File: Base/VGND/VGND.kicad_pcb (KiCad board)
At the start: 2 copper layers, 30 x 84 mm, 36 parts, among them J1 Barrel_Jack_Switch, J2 Conn_01x04_Pin, J3 Conn_01x05_Pin, J4 AudioJack2_Ground, J5 AudioJack2_Ground, Q1 40V, U1 TLE2426xD, U2 OPA1656

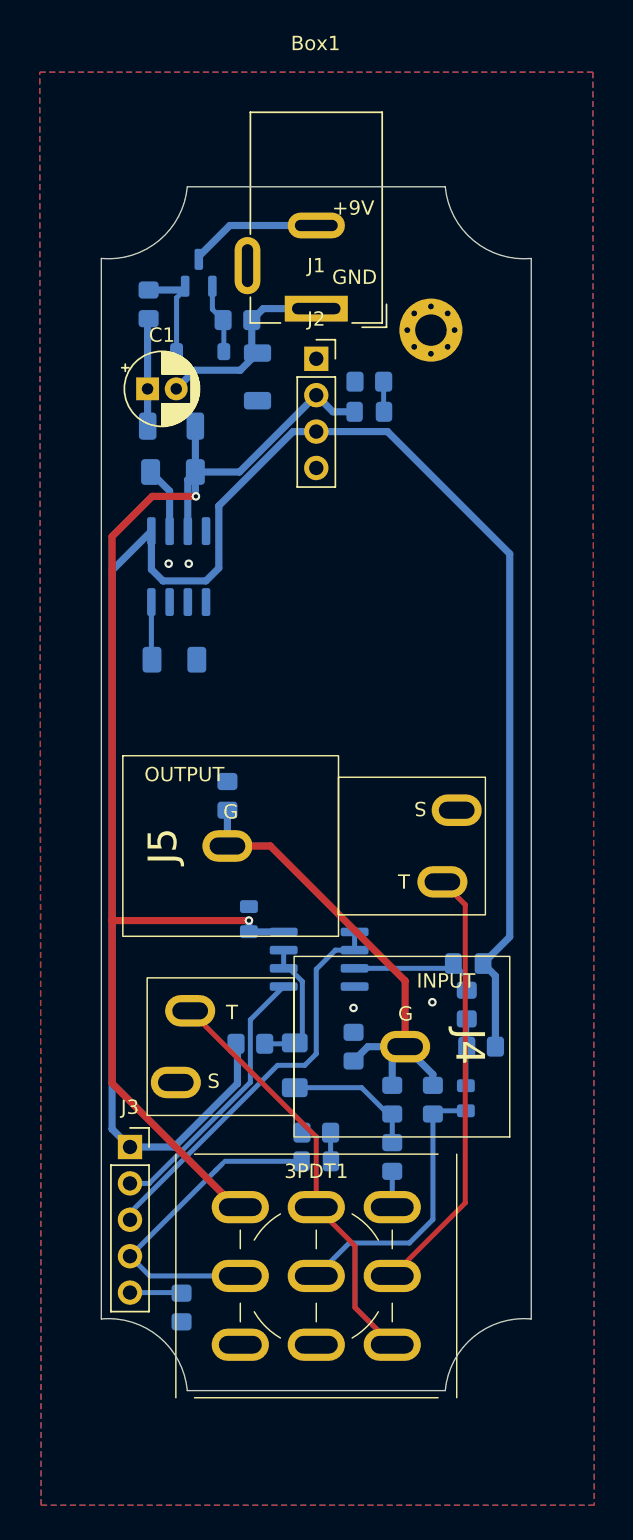
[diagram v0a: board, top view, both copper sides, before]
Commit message: VGND: misc KiCad-9 noise
Some manual via stitching - still waiting for the scripts to be updated
- and some library symbol changes that seem to be related to just minor
change sin KiCad 9.

Signed-off-by: Linus Torvalds <torvalds@linux-foundation.org>
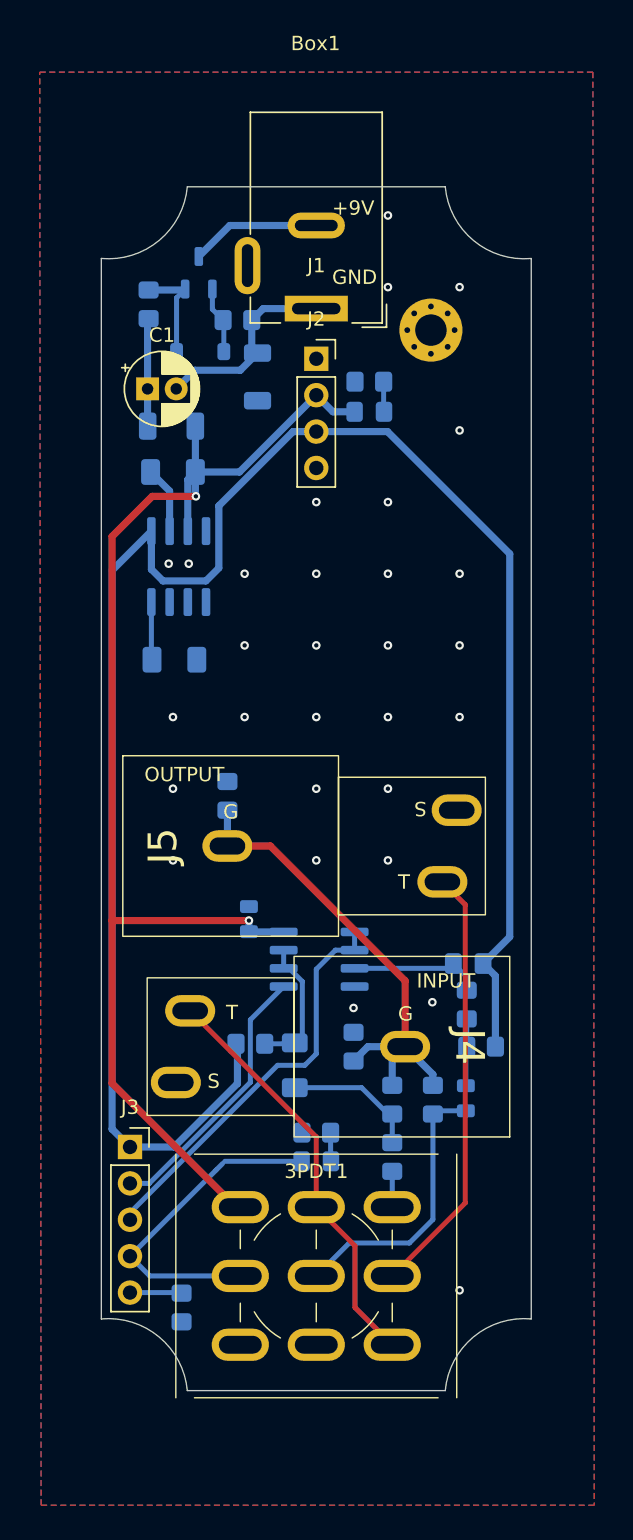
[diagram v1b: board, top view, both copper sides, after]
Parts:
- Q1: footprint Package_TO_SOT_SMD:SOT-23 -> Package_TO_SOT_SMD:SOT-23-3
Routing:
- net GND: vias 4 -> 30

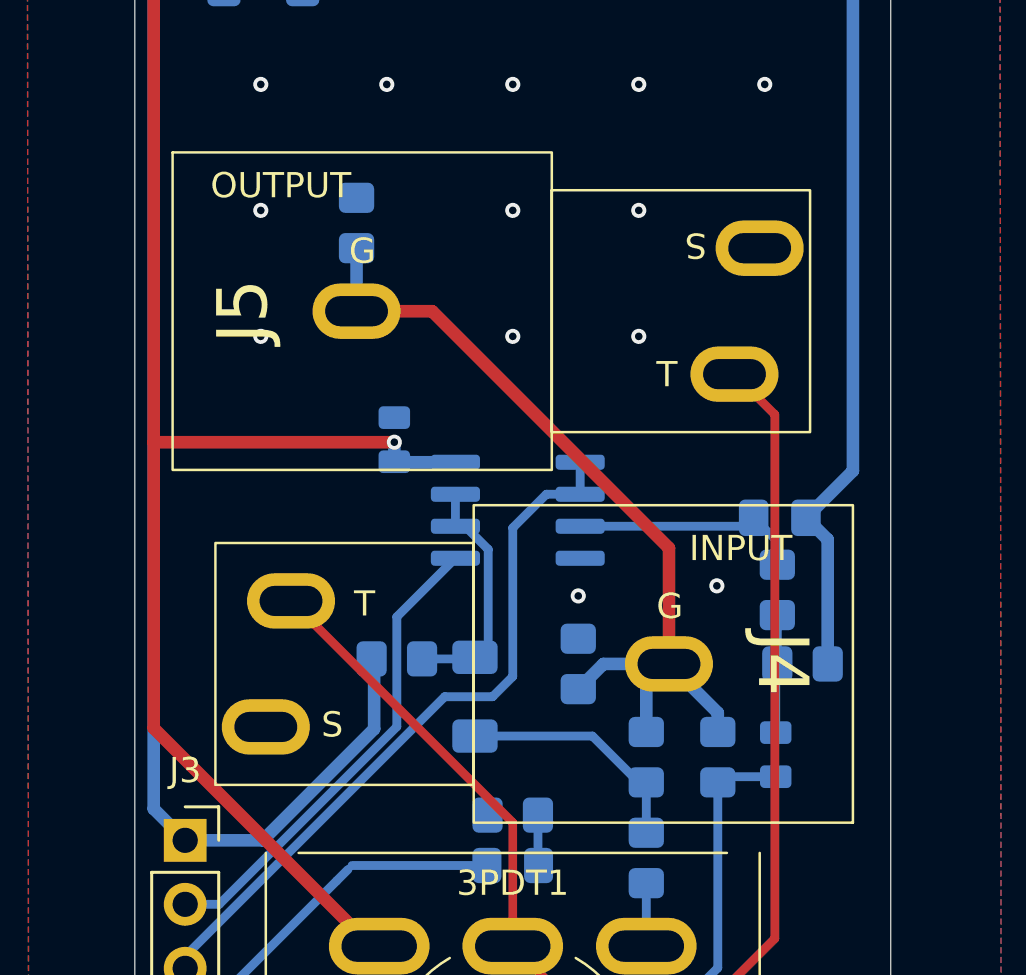
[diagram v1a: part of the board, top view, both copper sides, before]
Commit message: Move mono connectors out by 0.8mm each
Minimal trivial fixup to make the mono connectors poke out of the
enclosure just a tad more: this way we should have enough threads to
actually have the nut bite down on the jack.

Is the nut required? No.  But it should make things a bit stabler, and
let's do it right.

Is this enough? We'll see, but from a quick test-fit it looks just
barely sufficient, and I don't want to overdo it.

This is not worth doing new boards for, but I'm fixing it now so that
the next time I order more boards I will have this fixed.  I've meant to
do this for a long time, but just never got around to it.

Signed-off-by: Linus Torvalds <torvalds@linux-foundation.org>
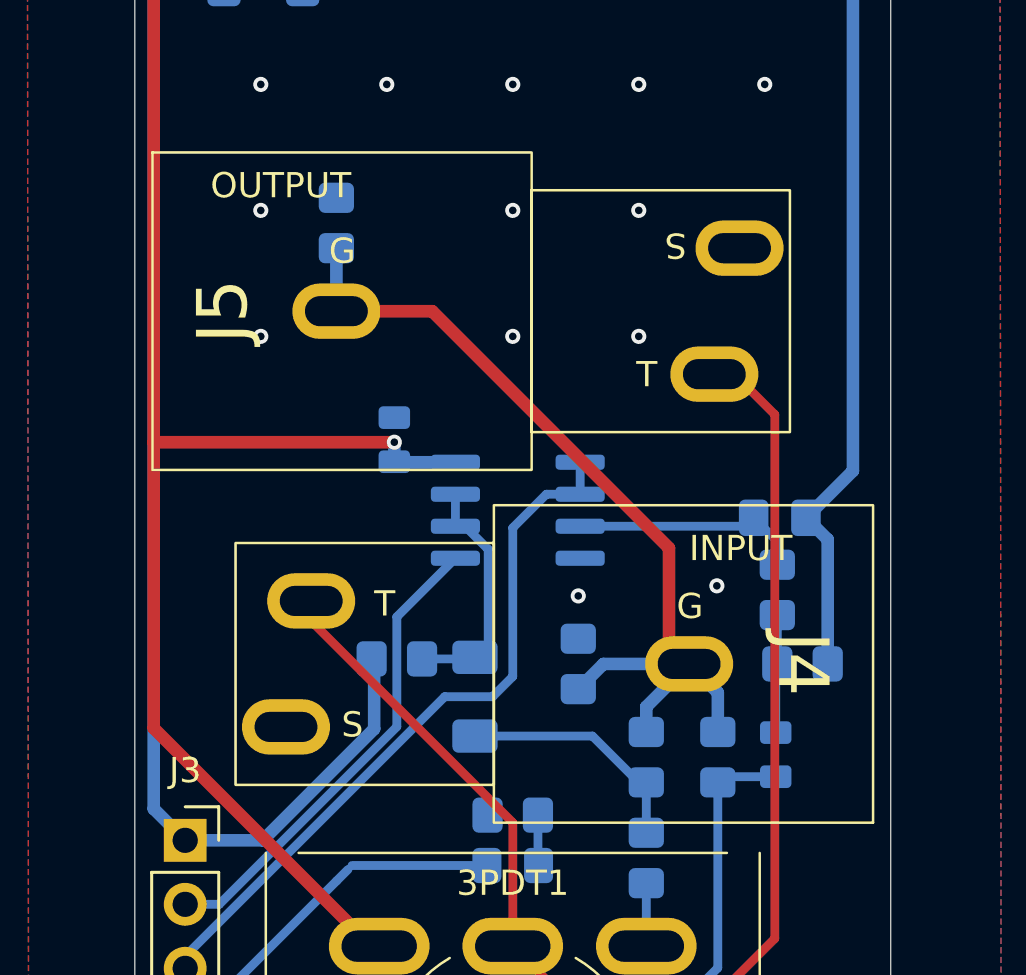
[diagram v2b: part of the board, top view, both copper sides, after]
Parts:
- moved J4 0.80 mm to (101.5, 118.0)
- moved J5 0.80 mm to (98.5, 104.0)
- moved R12 0.80 mm to (93.0, 100.5)
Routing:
- net GNDS: track 34.0 -> 34.8 mm
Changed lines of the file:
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@@
 	(footprint "Mylib:CK-6.35"
 		(layer "F.Cu")
-		(at 100.7 118 180)
+		(at 101.5 118 180)
 		(property "Reference" "J4"
 			(at -10 0 270)
@@
 	(footprint "Mylib:CK-6.35"
 		(layer "F.Cu")
-		(at 99.3 104)
+		(at 98.5 104)
 		(property "Reference" "J5"
 			(at -10 0 90)
@@
 	(footprint "Resistor_SMD:R_0805_2012Metric_Pad1.20x1.40mm_HandSolder"
 		(layer "B.Cu")
-		(at 93.8 100.5 -90)
+		(at 93 100.5 -90)
 		(descr "Resistor SMD 0805 (2012 Metric), square (rectangular) end terminal, IPC-7351 nominal with elongated pad for handsoldering. (Body size source: IPC-SM-782 page 72, https://www.pcb-3d.com/wordpress/wp-content/uploads/ipc-sm-782a_amendment_1_and_2.pdf), generated with kicad-footprint-generator")
 		(tags "resistor handsolder")
@@
 	)
 	(segment
-		(start 108.1375 119.9375)
-		(end 106.2 118)
+		(start 107 118)
+		(end 108.1375 119.1375)
 		(width 0.5)
 		(layer "B.Cu")
@@
 	)
 	(segment
-		(start 106.2 118)
-		(end 103.6 118)
+		(start 103.6 118)
+		(end 107 118)
 		(width 0.5)
 		(layer "B.Cu")
@@
 	)
 	(segment
-		(start 103.6 118)
-		(end 102.6 119)
+		(start 108.1375 119.1375)
+		(end 108.1375 120.7)
 		(width 0.5)
 		(layer "B.Cu")
@@
 	)
 	(segment
-		(start 105.3 118.9)
-		(end 106.2 118)
+		(start 103.6 118)
+		(end 102.6 119)
 		(width 0.5)
 		(layer "B.Cu")
@@
 	)
 	(segment
-		(start 108.1375 120.7)
-		(end 108.1375 119.9375)
+		(start 105.3 120.7)
+		(end 105.3 119.7)
 		(width 0.5)
 		(layer "B.Cu")
@@
 	)
 	(segment
-		(start 93.8 101.5)
-		(end 93.8 104)
+		(start 93 101.5)
+		(end 93 104)
 		(width 0.5)
 		(layer "B.Cu")
@@
 	)
 	(segment
-		(start 105.3 120.7)
-		(end 105.3 118.9)
+		(start 105.3 119.7)
+		(end 107 118)
 		(width 0.5)
 		(layer "B.Cu")

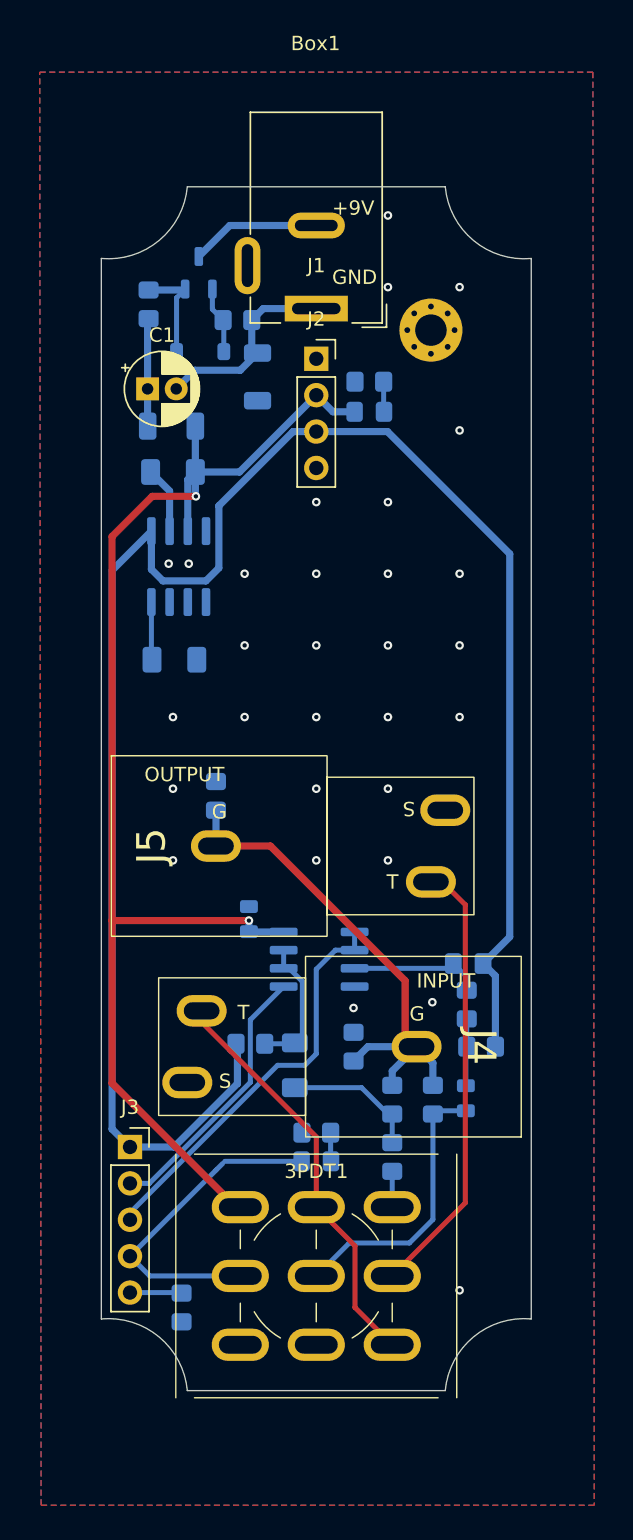
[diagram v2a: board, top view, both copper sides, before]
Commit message: Update the VGND board for things from the digital board
This brings the VGND board up to where the digital board was, and also
adds a common mode choke for more power cleaning testing (I know I said
I should do it for the USB-C power board, and I will, but I did it here
too just because I was updating things).

I think I'll try to actively hunt for a couple of cheap and hopefully
bad wall wart guitar power supplies.  Considering how many people
complain about bad guitar power supplies, it should hopefully be easy.

Will the choke matter? I have no idea, but hey, that's kind of the
point, isn't it?

This also adds in the simulation so that you can see the signal
rebiasing happening.  As usual ltspice randomly gives errors that come
and go depending on "use initial conditions" and timing, but when it
works it works.

Signed-off-by: Linus Torvalds <torvalds@linux-foundation.org>
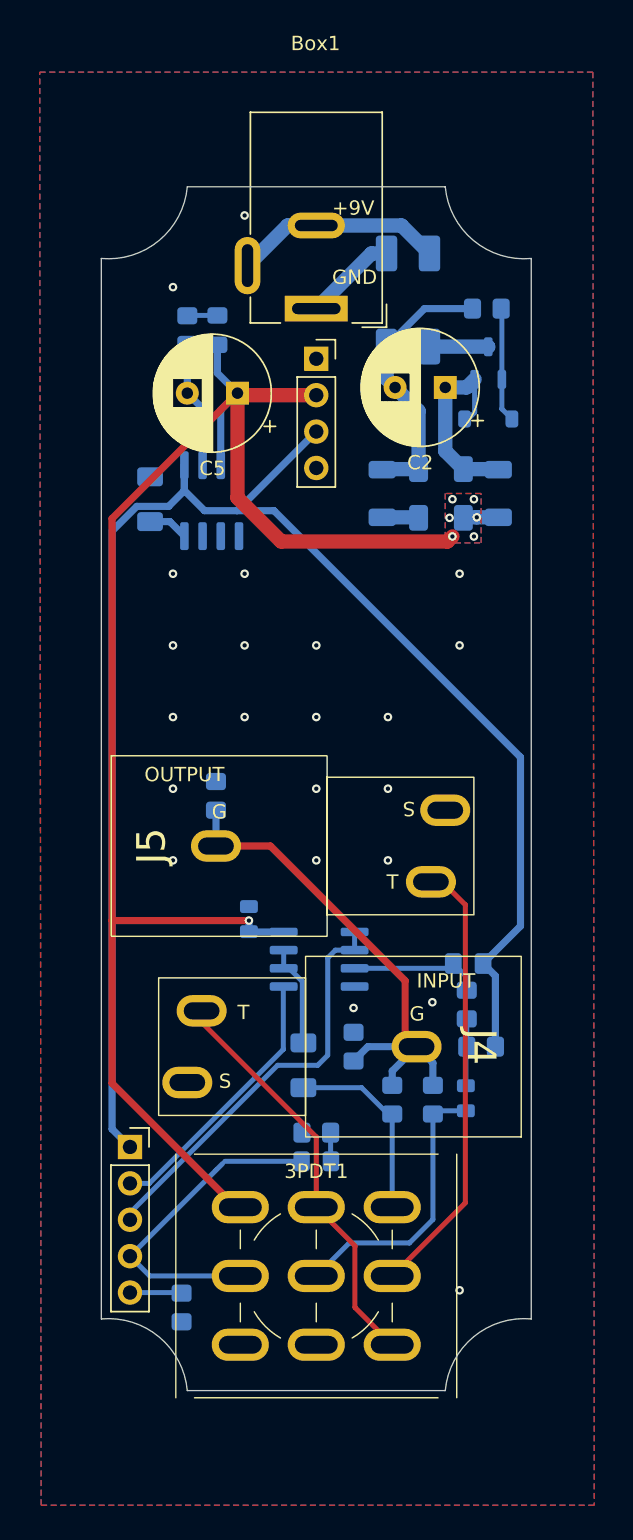
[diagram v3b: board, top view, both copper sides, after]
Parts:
- removed the C1 at (88.2, 72.1)
- removed H1: GroundingPad, MountingHole:MountingHole_2.2mm_M2_Pad_Via
- removed the R1 at (88.3, 66.2)
- removed the R6 at (105.3, 125.7)
- removed the R7 at (95.4, 117.8)
- added C2: 100uF, Capacitor_THT:CP_Radial_D8.0mm_P3.50mm, F.Cu at (109.0, 72.0)
- added C3: 10uF, Capacitor_SMD:C_1206_3216Metric_Pad1.33x1.80mm_HandSolder, B.Cu at (108.7, 77.7)
- added C5: 100uF, Capacitor_THT:CP_Radial_D8.0mm_P3.50mm, F.Cu at (94.5, 72.4)
- added FL1: ACM7060, Inductor_SMD:L_CommonModeChoke_TDK_ACM7060, B.Cu at (106.4, 65.9)
- C4: renamed from C2; value 47uF -> 10uF
- C9: renamed from C7; value 1uF -> 0.47uF
- R8: value 470k -> 100k
- moved FB1 23.3 mm to (112.7, 79.4), turned to -90 degrees
- moved Q1 21.2 mm to (112.0, 70.3)
- moved D1 20.6 mm to (112.0, 74.2)
- moved C4 19.0 mm to (108.7, 81.1)
- moved R1 17.4 mm to (111.9, 66.5), turned to 180 degrees
- moved R9 13.2 mm to (91.0, 68.0), turned to -90 degrees
- moved D2 12.0 mm to (93.1, 68.0), turned to -90 degrees
- moved FB2 11.9 mm to (104.6, 79.4)
- moved C1 11.3 mm to (88.4, 79.8), turned to 90 degrees
- moved U1 5.14 mm to (92.7, 79.9)
- moved C9 0.60 mm to (99.1, 119.3)
- renumbered C3 to C1, C5 to C6, C4 to C7, C6 to C8, J2 to J1, J3 to J2, J1 to J3, R2 to R1, R11 to R2, R12 to R6, R13 to R7
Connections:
- C9 pad 1: Net-(C7-Pad1) -> OUT^{RAW}
- FB1 pad 1: Net-(C1-Pad1) -> Net-(D1-K)
- J3 pad 1: GNDIN -> Net-(FL1-Pad1)
- J3 pad 2: +9V -> Net-(FL1-Pad2)
- J3 pad 3: unconnected-(J1-Pad3) -> Net-(FL1-Pad2)
- Q1 pad 3: +9V -> PWRIN
- R8 pad 1: Net-(C7-Pad1) -> OUT^{RAW}
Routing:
- net VIN: track 93.3 -> 118.1 mm, vias 2 -> 7
- net GNDREF: track 130.6 -> 113.9 mm
- net Net-(FL1-Pad2): track 0.00 -> 14.7 mm
- net OUT^{RAW}: track 2.50 -> 13.5 mm
- net Net-(C7-Pad1): track 9.56 -> 0.00 mm
- net +9V: track 9.10 -> 0.00 mm
- net Net-(C1-Pad1): track 7.42 -> 0.00 mm
- net Net-(D1-K): track 7.09 -> 14.2 mm
- net GND: track 4.67 -> 11.4 mm, vias 30 -> 22
- net Net-(FL1-Pad1): track 0.00 -> 6.49 mm
- net GNDIN: track 14.0 -> 19.1 mm
- net PWRIN: track 0.00 -> 4.11 mm
- net Net-(D1-A): track 4.62 -> 8.01 mm
- net Net-(U2B--): track 9.11 -> 6.88 mm
- net Net-(U1-NOISE_REDUCTION): track 3.98 -> 2.81 mm
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- added copper zone on B.Cu, net VIN
- added copper zone on F.Cu, net VIN
